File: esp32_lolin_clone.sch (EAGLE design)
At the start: 33 parts, among them J1 10104111-0001LF, P1 S2B-PH-SM4-TB, Q1 CJ2301S1, Q2 CJ2301S1, SW1 PTS815SJK250SMTR, U1 ESP32-WROOM-32D, U2 BCM857, U3 ME6211, U4 UMH3N, U5 TP4054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

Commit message: Routing and changing position of some components.
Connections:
- net N$11 renamed ESP32_EN
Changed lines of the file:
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@@
 </segment>
 </net>
-<net name="N$11" class="0">
+<net name="ESP32_EN" class="0">
 <segment>
 <pinref part="R1" gate="G$1" pin="2"/>

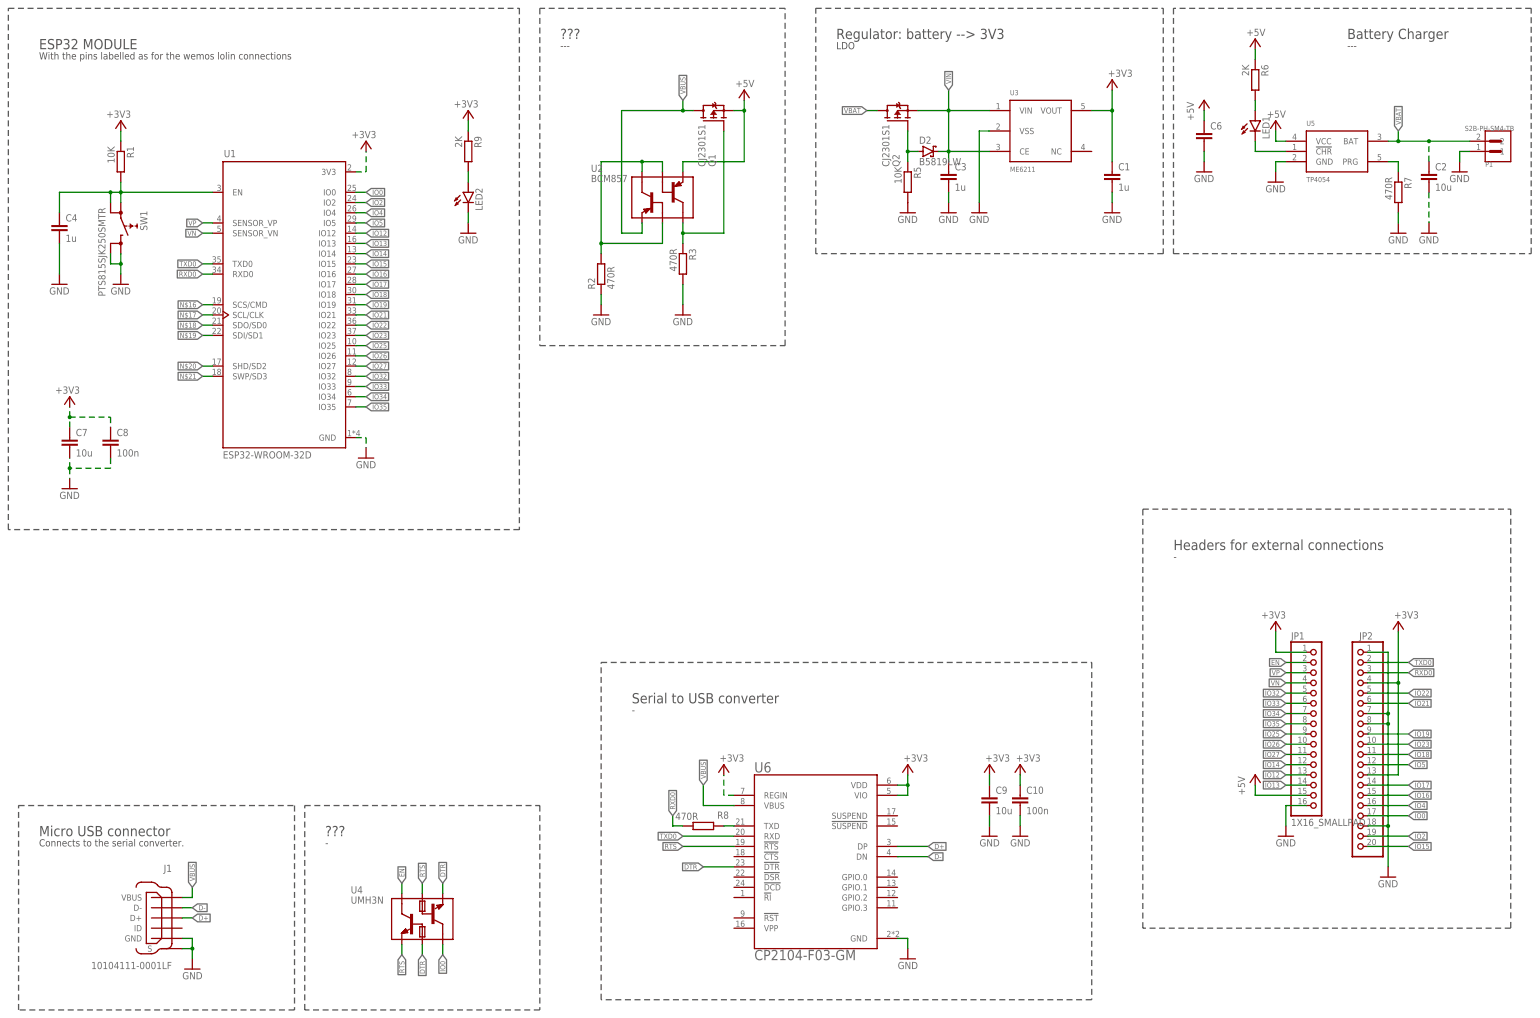
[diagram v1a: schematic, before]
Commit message: - Finish first routing attempt. - Add notes to schematic.
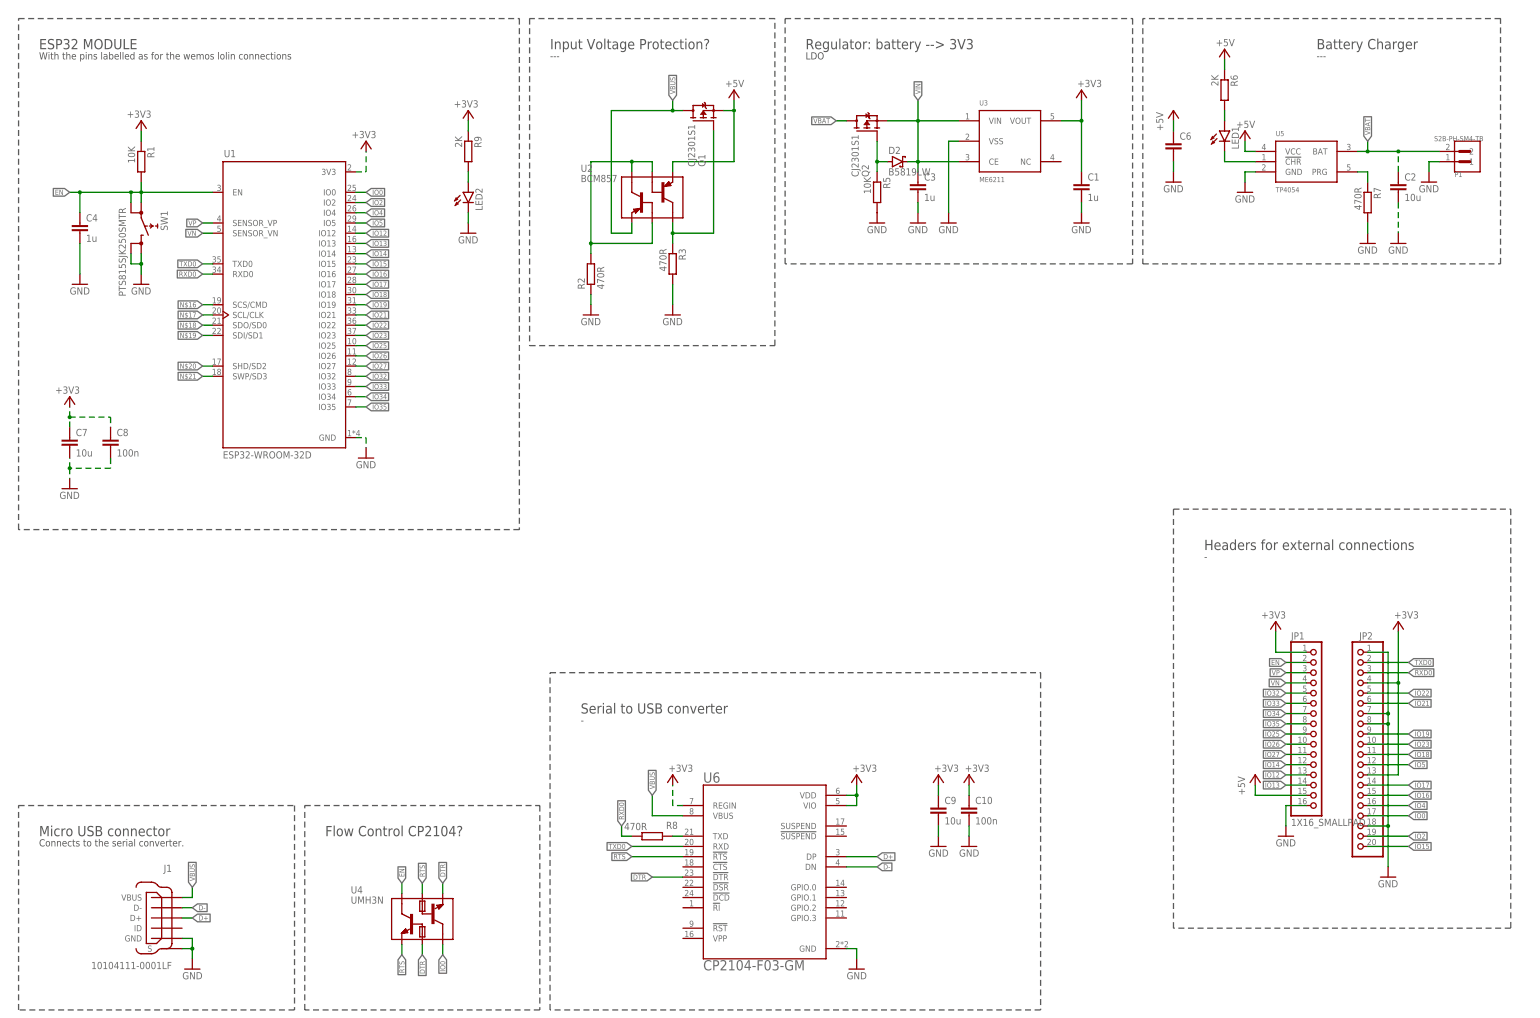
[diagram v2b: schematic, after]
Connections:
- removed net ESP32_EN: C4.1, R1.2, SW1.0@A, SW1.0@B, U1.EN
- net EN: now also C4.1, R1.2, SW1.0@A, SW1.0@B, U1.EN
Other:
- note added: "Flow Control CP2104?"
- note added: "Input Voltage Protection?"
- note removed: "???"
- moved on the sheet: C1, C10, C2, C3, C4, C6, C9, D2, LED1, P1, Q1, Q2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
